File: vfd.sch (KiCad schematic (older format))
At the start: 0 parts

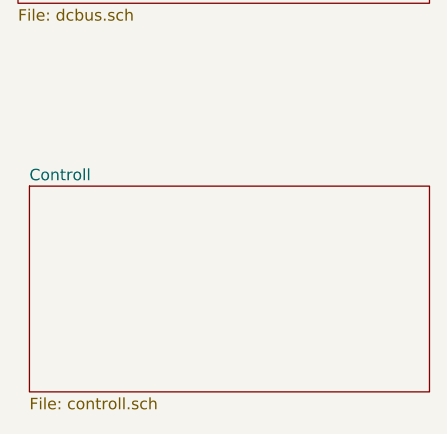
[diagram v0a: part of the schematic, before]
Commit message: started populating contoll part
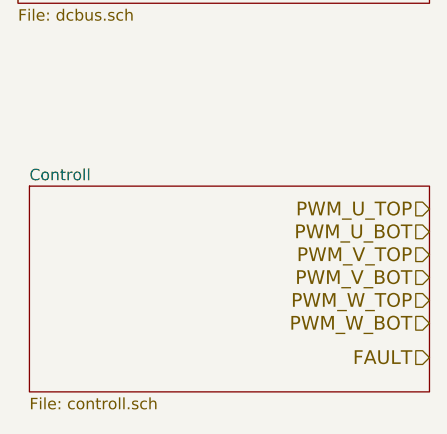
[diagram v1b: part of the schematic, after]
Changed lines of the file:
@@
 LIBS:valves
+LIBS:vfd-cache
 LIBS:vfd-cache
 EELAYER 24 0
@@
 F1 "controll.sch" 50
 $EndSheet
+Text HLabel 3250 3200 0    60   Input ~ 0
+PWM_U_TOP
+Text HLabel 3250 3300 0    60   Input ~ 0
+PWM_U_BOT
+Text HLabel 3250 3500 0    60   Input ~ 0
+PWM_V_BOT
+Text HLabel 3250 3400 0    60   Input ~ 0
+PWM_V_TOP
+Text HLabel 3250 3700 0    60   Input ~ 0
+PWM_W_BOT
+Text HLabel 3250 3600 0    60   Input ~ 0
+PWM_W_TOP
+Text HLabel 3250 3850 0    60   Input ~ 0
+FAULT
 $EndSCHEMATC

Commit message: begin working on output power stage
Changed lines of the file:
@@
 $Descr A4 11693 8268
 encoding utf-8
-Sheet 1 3
+Sheet 1 5
 Title ""
 Date ""
@@
 $EndDescr
 $Sheet
-S 1450 1400 1800 900
+S 2500 1300 1800 900
 U 5377D90A
 F0 "DC Bus" 50
 F1 "dcbus.sch" 50
-F2 "DCBUS" I R 3250 1550 60
-F3 "GND" I R 3250 1950 60
-F4 "EARTH" I L 1450 2200 60
+F2 "DCBUS" I R 4300 1450 60
+F3 "GND" I L 2500 1950 60
+F4 "EARTH" I L 2500 2100 60
+F5 "DCBUSSENSE" I R 4300 2050 60
 $EndSheet
 $Sheet
-S 1500 3100 1750 900
+S 2550 3000 1750 1400
 U 537BA57E
 F0 "Controll" 50
 F1 "controll.sch" 50
+F2 "PWM_U_TOP" I R 4300 3050 60
+F3 "PWM_U_BOT" I R 4300 3150 60
+F4 "PWM_V_TOP" I R 4300 3250 60
+F5 "PWM_V_BOT" I R 4300 3350 60
+F6 "PWM_W_TOP" I R 4300 3450 60
+F7 "PWM_W_BOT" I R 4300 3550 60
+F8 "DCBUSSENSE" I R 4300 4100 60
+F9 "RBRAKE" I R 4300 4200 60
+F10 "ACCEL" I L 2550 3050 60
+F11 "SPEED" I L 2550 3150 60
+F12 "~START" I L 2550 3250 60
+F13 "~FWD" I L 2550 3350 60
+F14 "TXD" I L 2550 3700 60
+F15 "RXD" I L 2550 3800 60
+F16 "FAULT" I R 4300 4000 60
+F17 "+5V" I L 2550 4100 60
+F18 "GND" I L 2550 4200 60
 $EndSheet
-Text HLabel 3250 3200 0    60   Input ~ 0
-PWM_U_TOP
-Text HLabel 3250 3300 0    60   Input ~ 0
-PWM_U_BOT
-Text HLabel 3250 3500 0    60   Input ~ 0
-PWM_V_BOT
-Text HLabel 3250 3400 0    60   Input ~ 0
-PWM_V_TOP
-Text HLabel 3250 3700 0    60   Input ~ 0
-PWM_W_BOT
-Text HLabel 3250 3600 0    60   Input ~ 0
-PWM_W_TOP
-Text HLabel 3250 3850 0    60   Input ~ 0
-FAULT
+$Sheet
+S 2600 5300 1700 1250
+U 5389A5FF
+F0 "Controll-pannel" 60
+F1 "controll_pannel.sch" 60
+F2 "ACCEL" I L 2600 5700 60
+F3 "SPEED" I L 2600 5600 60
+F4 "~START" I L 2600 5500 60
+F5 "~FWD" I L 2600 5400 60
+F6 "+5V" I L 2600 6100 60
+F7 "GND" I L 2600 6200 60
+$EndSheet
+Wire Wire Line
+	4300 2050 4700 2050
+Wire Wire Line
+	4700 2050 4700 4100
+Wire Wire Line
+	4700 4100 4300 4100
+Wire Wire Line
+	2500 1950 1800 1950
+Wire Wire Line
+	1800 1950 1800 6200
+Wire Wire Line
+	1800 4200 2550 4200
+Wire Wire Line
+	1800 6200 2600 6200
+Connection ~ 1800 4200
+Wire Wire Line
+	2600 6100 1900 6100
+Wire Wire Line
+	1900 6100 1900 4100
+Wire Wire Line
+	1900 4100 2550 4100
+Wire Wire Line
+	2550 3350 2350 3350
+Wire Wire Line
+	2350 3350 2350 5400
+Wire Wire Line
+	2350 5400 2600 5400
+Wire Wire Line
+	2550 3250 2250 3250
+Wire Wire Line
+	2250 3250 2250 5500
+Wire Wire Line
+	2250 5500 2600 5500
+Wire Wire Line
+	2550 3150 2150 3150
+Wire Wire Line
+	2150 3150 2150 5600
+Wire Wire Line
+	2150 5600 2600 5600
+Wire Wire Line
+	2550 3050 2050 3050
+Wire Wire Line
+	2050 3050 2050 5700
+Wire Wire Line
+	2050 5700 2600 5700
+$Sheet
+S 7100 2200 2900 2250
+U 538A160F
+F0 "Power output stage" 60
+F1 "output.sch" 60
+F2 "W" I R 10000 2650 60
+F3 "V" I R 10000 2850 60
+F4 "U" I R 10000 3050 60
+$EndSheet
 $EndSCHEMATC

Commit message: populating boards
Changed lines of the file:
@@
-$EndSheet
-$Sheet
-S 2550 3000 1750 1400
-U 537BA57E
-F0 "Controll" 50
-F1 "controll.sch" 50
-F2 "PWM_U_TOP" I R 4300 3050 60
-F3 "PWM_U_BOT" I R 4300 3150 60
-F4 "PWM_V_TOP" I R 4300 3250 60
-F5 "PWM_V_BOT" I R 4300 3350 60
-F6 "PWM_W_TOP" I R 4300 3450 60
-F7 "PWM_W_BOT" I R 4300 3550 60
-F8 "DCBUSSENSE" I R 4300 4100 60
-F9 "RBRAKE" I R 4300 4200 60
-F10 "ACCEL" I L 2550 3050 60
-F11 "SPEED" I L 2550 3150 60
-F12 "~START" I L 2550 3250 60
-F13 "~FWD" I L 2550 3350 60
-F14 "TXD" I L 2550 3700 60
-F15 "RXD" I L 2550 3800 60
-F16 "FAULT" I R 4300 4000 60
-F17 "+5V" I L 2550 4100 60
-F18 "GND" I L 2550 4200 60
 $EndSheet
 $Sheet
@@
 Wire Wire Line
 	4300 2050 4700 2050
-Wire Wire Line
-	4700 2050 4700 4100
-Wire Wire Line
-	4700 4100 4300 4100
 Wire Wire Line
 	2500 1950 1800 1950
@@
 	2050 5700 2600 5700
 $Sheet
-S 7100 2200 2900 2250
+S 6700 2150 2900 2250
 U 538A160F
 F0 "Power output stage" 60
 F1 "output.sch" 60
-F2 "W" I R 10000 2650 60
-F3 "V" I R 10000 2850 60
-F4 "U" I R 10000 3050 60
+F2 "W" I R 9600 2600 60
+F3 "V" I R 9600 2800 60
+F4 "U" I R 9600 3000 60
+F5 "PWM_U_TOP" I L 6700 2300 60
+F6 "PWM_V_TOP" I L 6700 2400 60
+F7 "PWM_W_TOP" I L 6700 2500 60
+F8 "PWM_U_BOT" I L 6700 2700 60
+F9 "PWM_V_BOT" I L 6700 2800 60
+F10 "PWM_W_BOT" I L 6700 2900 60
+F11 "W_CURRENT" I L 6700 3300 60
+F12 "V_CURRENT" I L 6700 3200 60
+F13 "U_CURRENT" I L 6700 3100 60
+F14 "DCBUS" I R 9600 2300 60
+F15 "GND" I R 9600 4250 60
+F16 "FAULT" I L 6700 3900 60
+F17 "SHORT_PROTECT" I L 6700 4050 60
 $EndSheet
+$Sheet
+S 2550 3000 1750 1400
+U 537BA57E
+F0 "Controll" 50
+F1 "controll.sch" 50
+F2 "PWM_U_TOP" I R 4300 3050 60
+F3 "PWM_U_BOT" I R 4300 3400 60
+F4 "PWM_V_TOP" I R 4300 3150 60
+F5 "PWM_V_BOT" I R 4300 3500 60
+F6 "PWM_W_TOP" I R 4300 3250 60
+F7 "PWM_W_BOT" I R 4300 3600 60
+F8 "DCBUSSENSE" I R 4300 3950 60
+F9 "RBRAKE" I R 4300 4100 60
+F10 "ACCEL" I L 2550 3050 60
+F11 "SPEED" I L 2550 3150 60
+F12 "~START" I L 2550 3250 60
+F13 "~FWD" I L 2550 3350 60
+F14 "TXD" I L 2550 3700 60
+F15 "RXD" I L 2550 3800 60
+F16 "FAULT" I R 4300 3800 60
+F17 "+5V" I L 2550 4100 60
+F18 "GND" I L 2550 4200 60
+$EndSheet
+Wire Wire Line
+	4300 3950 4700 3950
+Wire Wire Line
+	4700 3950 4700 2050
 $EndSCHEMATC
